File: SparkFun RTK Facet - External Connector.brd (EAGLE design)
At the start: 50 x 20 mm, 51 parts, among them J1 Qwiic, J3 ESP32 USB, J4 Qwiic, J5 u-blox USB

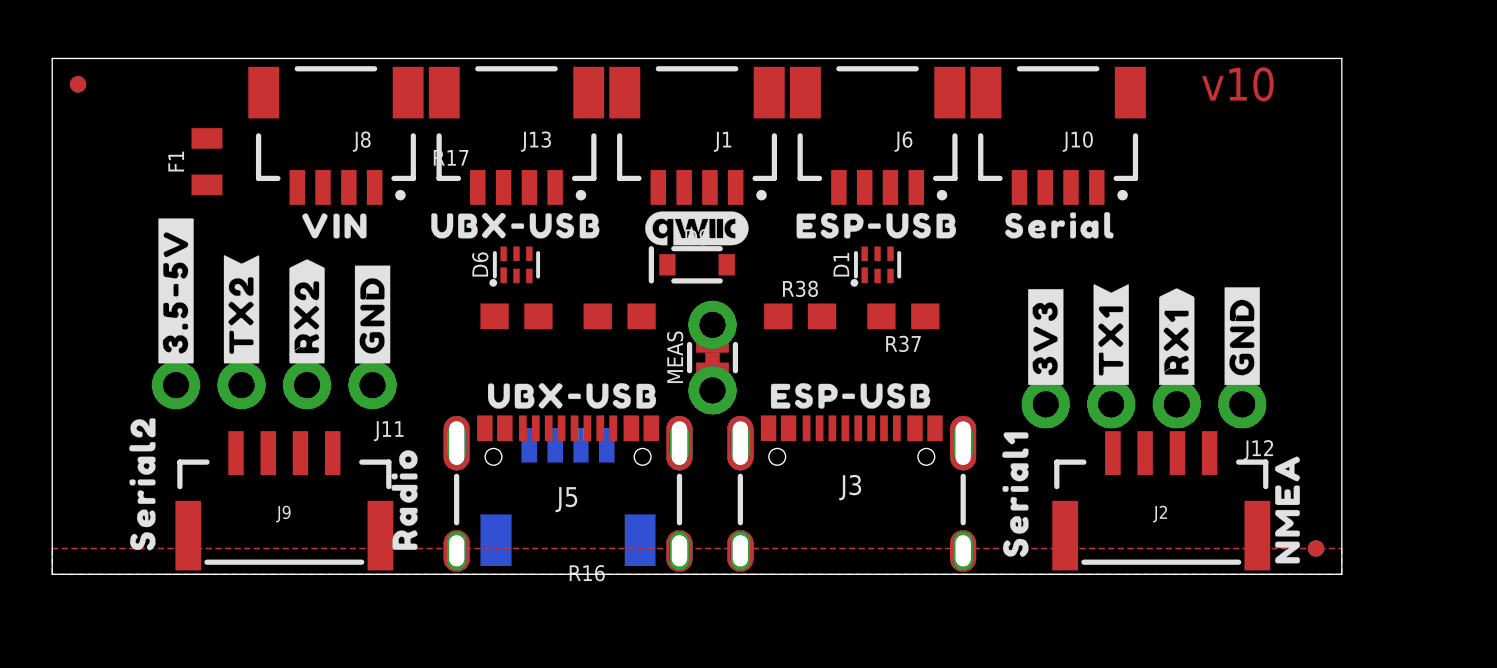
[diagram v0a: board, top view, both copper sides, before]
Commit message: Add 22ohm to USB hub D+/D-.
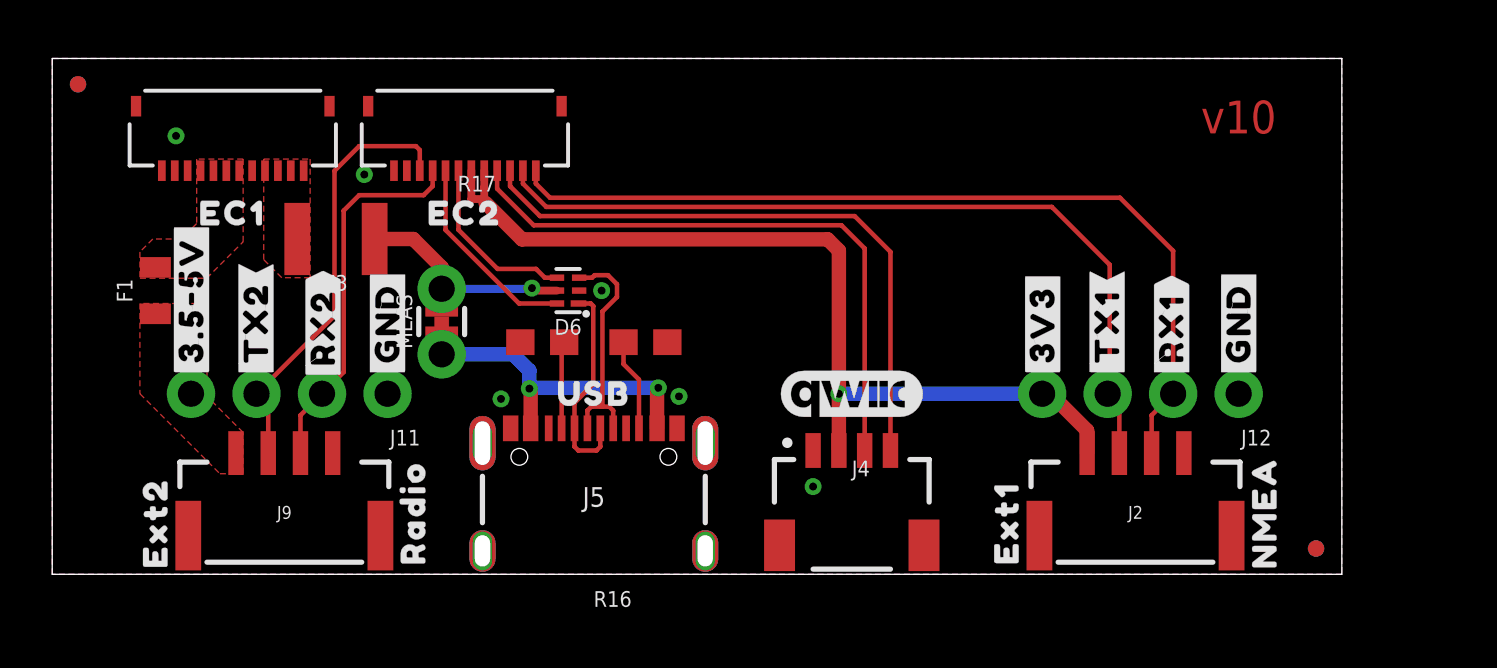
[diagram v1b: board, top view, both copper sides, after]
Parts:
- removed D1: PRTR5V0U2F, SparkFun-IC-Power:SOT886
- removed D9: 3A/10V/280mV, SparkFun-DiscreteSemi:SOD-323
- removed J1: Qwiic, SparkFun-Connectors:JST04_1MM_RA
- removed J10, J13, J8: (no value), SparkFun-Connectors:JST04_1MM_RA
- removed R37, R38: 5.1k, SparkFun-Resistors:0603
- removed U$29: (no value), output:SERIAL10
- removed U$3: (no value), output:SERIAL3
- removed U$30: (no value), SparkFun-Aesthetics:QWIIC_4MM
- removed U$43: (no value), output:SERIAL20
- removed U$49: (no value), output:NMEA1
- removed U$50: (no value), output:RADIO0
- added F3: 6V/2A, SparkFun-Fuses:1210
- added U$11: (no value), output:EC21
- added U$12: (no value), output:RADIO3
- J3: value ESP32 USB -> FPC_12_0.5MM2; device SparkFun-Connectors:USB-C-16P-2LAYER-PADS -> RTK Facet:FPC_12_FLIP_DOUBLESIDED_2
- J6: value (none) -> FPC_12_0.5MM2; device SparkFun-Connectors:JST04_1MM_RA -> RTK Facet:FPC_12_FLIP_DOUBLESIDED_2
- U$1: device output:ESP#USB0 -> output:USB0
- U$4: device output:UBX#USB1 -> output:EXT10
- U$6: device output:VIN2 -> output:EXT22
- U$7: device output:UBX#USB1 -> output:NMEA1
- U$8: device output:ESP#USB0 -> output:EC10
- moved U$7 27.2 mm to (47.0, 2.40), turned to 90 degrees
- moved J6 25.1 mm to (7.00, 17.0)
- moved U$8 25.0 mm to (7.00, 14.0)
- moved U$4 22.2 mm to (37.0, 2.00), turned to 90 degrees
- moved J3 18.6 mm to (16.0, 17.0), turned to 180 degrees
- moved U$6 13.5 mm to (4.00, 2.00), turned to 90 degrees
- moved U$1 12.8 mm to (21.0, 7.00)
- moved J4 11.0 mm to (31.0, 4.80), flipped to the top
- moved LOGO3 11.0 mm to (31.0, 7.00), flipped to the top
- moved MEAS 10.6 mm to (15.1, 9.80)
- moved F1 5.39 mm to (4.00, 11.0)
- moved D6 2.24 mm to (20.0, 11.0), turned to 180 degrees
- moved R16 1.41 mm to (23.0, 9.00)
- moved R17 1.41 mm to (19.0, 9.00)
- moved J2 1.00 mm to (42.0, 1.40)
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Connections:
- net UBX1_D_N renamed USB1_D_M
- net UBX1_D_P renamed USB1_D_P
- removed net CC3: J3.B5, R37.2
- removed net CC4: J3.A5, R38.2
- removed net ESP1_D_N: D1.1, J3.A7, J3.B7
- removed net ESP1_D_P: D1.3, J3.A6, J3.B6
- removed net ESP_D_N: D1.6, J6.3
- removed net ESP_D_P: D1.4, J6.2
- removed net N$32: D9.A, J3.VBUS1, J3.VBUS2
- removed net UBX_D_N: D6.6, J13.3
- removed net UBX_D_P: D6.4, J13.2
- removed net VIN: D1.5, D6.5, D9.C, J13.1, J6.1, MEAS.2, MEAS.4
- new net N$1: D6.5, F3.1, MEAS.2, MEAS.4
- new net USB_DM: D6.6, J3.8
- new net USB_DP: D6.4, J3.7
- new net V_USB: F3.2, J6.1, J6.2, J6.3, J6.4
- net 3.3V: now also J3.5, J3.6; no longer J1.2
- net ESP_21/SDA: now also J3.4; no longer J1.3
- net ESP_22/SCL: now also J3.3; no longer J1.4
- net EXTERNAL_SERIAL1_RXI: now also J3.1; no longer J10.1
- net EXTERNAL_SERIAL1_TXO: now also J3.2; no longer J10.2
- net GND: now also J3.11, J3.12, J6.10, J6.11, J6.12; no longer D1.2, J1.1, J13.4, J3.GND, J3.GND2, J3.SHLD1, J3.SHLD2, J3.SHLD3, J3.SHLD4, J6.4, J8.1, J8.2, R37.1, R38.1
- net V_BATT: now also J6.6, J6.7, J6.8, J6.9; no longer J8.3, J8.4
- net ZED-RXI2: now also J3.9; no longer J10.3
- net ZED-TXO2: now also J3.10; no longer J10.4
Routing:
- net 3.3V: track 0.00 -> 36.3 mm, vias 0 -> 1
- net EXTERNAL_SERIAL1_RXI: track 0.00 -> 34.5 mm
- net EXTERNAL_SERIAL1_TXO: track 0.00 -> 32.1 mm
- net ESP_22/SCL: track 0.00 -> 24.1 mm
- net ESP_21/SDA: track 0.00 -> 23.7 mm
- net ZED-TXO2: track 0.00 -> 16.9 mm
- net ZED-RXI2: track 0.00 -> 14.5 mm
- net N$4: track 0.00 -> 13.3 mm, vias 0 -> 2
- net N$1: track 0.00 -> 9.57 mm, vias 0 -> 1
- net USB1_D_P: track 0.00 -> 9.17 mm
- net USB1_D_M: track 0.00 -> 8.20 mm
- net USB_DM: track 0.00 -> 7.80 mm
- net USB_DP: track 0.00 -> 6.88 mm
- net CC2: track 0.00 -> 3.59 mm
- net CC1: track 0.00 -> 3.38 mm
- added copper zone on layer 1, net N$3
- added copper zone on layer 1, net V_BATT
- added copper zone on layer 1, net V_USB
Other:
- board text removed: "4 Layer Board"
- board text removed: "No clean process"

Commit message: Fix errors on all 3 boards after enclosure review.
* Flip connector board completely. Mirror connectors.
* Mirror connector on SD board
* Move LED above SIM socket
* Add membrane connector to SD board
* Remove switch connector from main board
* Increase width of connector board, 2mm on each side - 54mm wide
* Move LiPo Connector north as much as possible
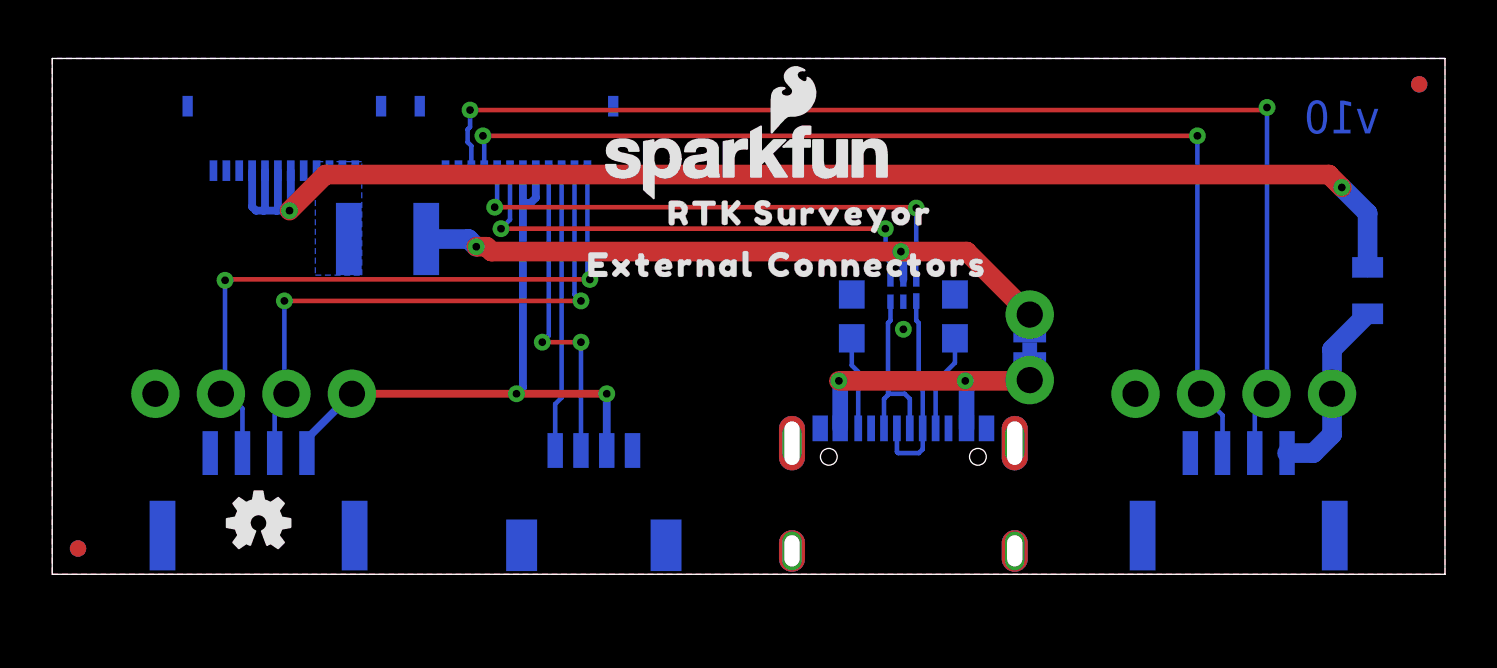
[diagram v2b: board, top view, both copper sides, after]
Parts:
- removed J3: FPC_12_0.5MM2, RTK Facet:FPC_12_FLIP_DOUBLESIDED_2
- added J1: FPC_12_0.5MM2, RTK Facet:FPC_12_FLIP_DOUBLESIDED_2
- moved JP61 52.0 mm to (53.0, 19.0), flipped to the bottom
- moved JP81 52.0 mm to (53.0, 19.0), flipped to the top
- moved JP21 48.0 mm to (1.00, 1.00), flipped to the bottom
- moved JP71 48.0 mm to (1.00, 1.00), flipped to the top
- moved F1 47.0 mm to (51.0, 11.0), flipped to the bottom
- moved U$6 47.0 mm to (51.0, 2.00), flipped to the bottom
- moved U$23 44.2 mm to (49.6, 7.50), flipped to the bottom
- moved U$7 44.0 mm to (3.00, 2.40), flipped to the bottom
- moved J12 42.0 mm to (4.00, 7.00), flipped to the bottom
- moved U$82 42.0 mm to (4.00, 7.50), flipped to the bottom
- moved U$40 39.2 mm to (47.1, 7.50), flipped to the bottom
- moved J9 37.0 mm to (46.0, 1.40), flipped to the bottom
- moved U$68 36.8 mm to (6.60, 7.50), flipped to the bottom
- moved J2 34.0 mm to (8.00, 1.40), flipped to the bottom
- moved LOGO1 34.0 mm to (8.00, 2.00), flipped to the top
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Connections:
- net N$1 renamed VIN1
- net N$4 renamed VIN
- net 3.3V: now also J6.7, J6.8; no longer J3.5, J3.6
- net ESP_21/SDA: now also J6.9; no longer J3.4
- net ESP_22/SCL: now also J6.10; no longer J3.3
- net EXTERNAL_SERIAL1_RXI: now also J6.12; no longer J3.1
- net EXTERNAL_SERIAL1_TXO: now also J6.11; no longer J3.2
- net GND: now also J1.1, J1.2, J1.3, J6.1, J6.2; no longer J3.11, J3.12, J6.10, J6.11, J6.12
- net USB_DM: now also J6.5; no longer J3.8
- net USB_DP: now also J6.6; no longer J3.7
- net V_BATT: now also J1.4, J1.5, J1.6, J1.7; no longer J6.6, J6.7, J6.8, J6.9
- net V_USB: now also J1.10, J1.11, J1.12, J1.9; no longer J6.1, J6.2, J6.3, J6.4
- net ZED-RXI2: now also J6.4; no longer J3.9
- net ZED-TXO2: now also J6.3; no longer J3.10
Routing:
- net V_BATT: track 0.00 -> 52.7 mm, vias 0 -> 2
- net ZED-TXO2: track 16.9 -> 47.0 mm, vias 0 -> 2
- net ZED-RXI2: track 14.5 -> 41.8 mm, vias 0 -> 2
- net VIN1: track 9.57 -> 26.5 mm, vias 1 -> 2
- net ESP_22/SCL: track 24.1 -> 11.0 mm
- net USB_DM: track 7.80 -> 20.6 mm, vias 0 -> 2
- net USB_DP: track 6.88 -> 19.3 mm, vias 0 -> 2
- net ESP_21/SDA: track 23.7 -> 12.5 mm, vias 0 -> 2
- net 3.3V: track 36.3 -> 25.5 mm, vias 1 -> 2
- net EXTERNAL_SERIAL1_TXO: track 32.1 -> 22.8 mm, vias 0 -> 2
- net EXTERNAL_SERIAL1_RXI: track 34.5 -> 25.6 mm, vias 0 -> 2
- net N$3: track 0.00 -> 7.29 mm
- net USB1_D_P: track 9.17 -> 7.10 mm
- net VIN: track 13.3 -> 11.9 mm
- added copper zone on layer 16, net V_USB
- removed copper zone on layer 1, net N$3
- removed copper zone on layer 1, net V_BATT
- removed copper zone on layer 1, net V_USB
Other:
- board size 50 x 20 mm -> 54 x 20 mm
